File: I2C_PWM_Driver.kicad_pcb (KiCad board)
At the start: 2 copper layers, 89 x 42 mm, 97 parts, among them J1 Screw_Terminal_01x02, J2 Conn_01x02_Male, J3 Screw_Terminal_01x02, J4 Conn_02x08_Odd_Even, Q1 DMG2305UX, Q10 DMG2305UX, Q11 BC817, Q12 BC817, Q13 DMG2305UX, Q14 DMG2305UX, Q15 BC817, Q16 BC817, Q17 DMG2305UX, Q18 DMG2305UX, Q19 BC817, Q2 DMG2305UX, Q20 BC817, Q21 DMG2305UX, Q22 DMG2305UX, Q23 BC817, Q24 BC817, Q25 DMG2305UX, Q26 DMG2305UX, Q27 BC817, Q28 BC817, Q29 DMG2305UX, Q3 BC817, Q30 DMG2305UX, Q31 BC817, Q32 BC817, Q4 BC817, Q5 DMG2305UX, Q6 DMG2305UX, Q7 BC817, Q8 BC817, Q9 DMG2305UX, SW1 SW_Push, U1 PCA9685PW, U2 LM2931-5.0_SO8

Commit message: Silk updates
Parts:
- J3: footprint PWM_Conn:SCREW TERMINAL BLOCK 3.5MM 2POS -> Connector_PinHeader_2.54mm:PinHeader_1x02_P2.54mm_Vertical
- moved REF** 8.62 mm to (147.4, 87.4)
- moved J3 4.00 mm to (77.8, 80.3), turned to 0 degrees
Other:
- board text added: "+"
- board text added: "-"
- board text added: "0"
- board text added: "1"
- board text added: "10"
- board text added: "11"
- board text added: "12"
- board text added: "13"
- board text added: "14"
- board text added: "15"
- board text added: "2"
- board text added: "3"
- board text added: "4"
- board text added: "5"
- board text added: "6"
- board text added: "7"
- board text added: "8"
- board text added: "9"
- board text added: "PWM Out+"
- board text added: "SCL"
- board text added: "SDA"
- board text added: "Vin"

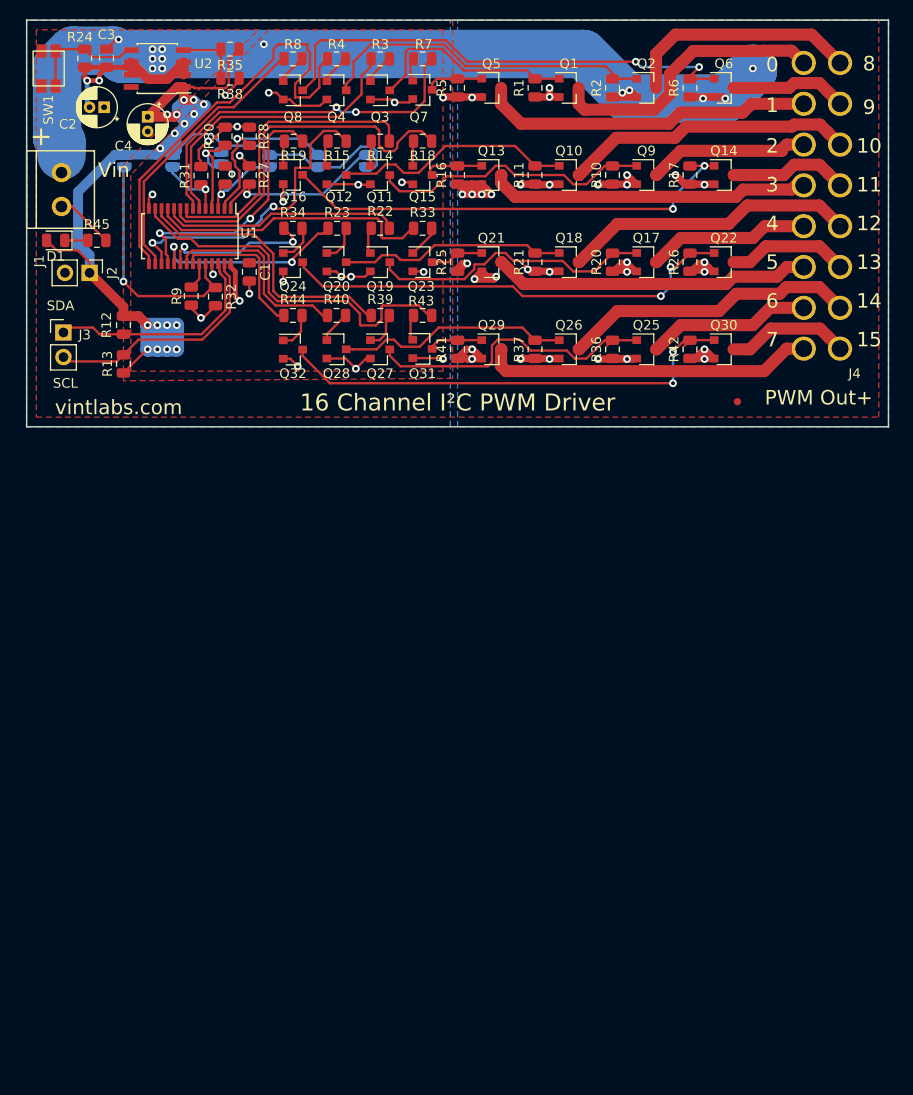
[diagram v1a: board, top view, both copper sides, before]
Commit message: Minmor silk updates
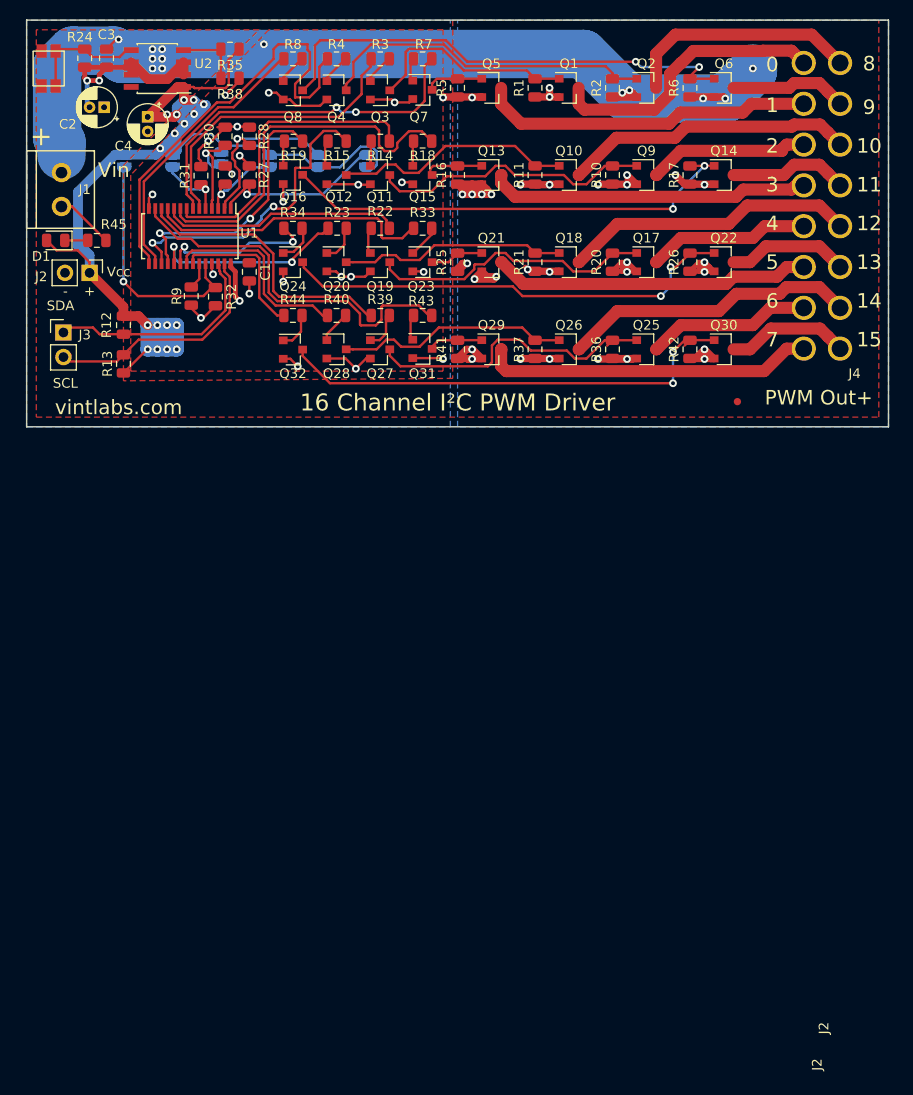
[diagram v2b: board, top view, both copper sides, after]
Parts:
- added ? (x2): , , F.Cu at (78.0, 76.0)
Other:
- board text added: "Vcc"
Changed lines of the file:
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@@
   (general
     (thickness 1.6)
-    (drawings 44)
+    (drawings 47)
     (tracks 1026)
     (zones 0)
-    (modules 97)
+    (modules 99)
     (nets 80)
   )
@@
     (add_net VCC)
   )
+  (module "" (layer F.Cu)
+    (at 78 76)
+    (fp_text reference "" (at 78 76) (layer F.SilkS)
+      (effects (font (size 1.27 1.27) (thickness 0.15)))
+    )
+    (fp_text value "" (at 78 76) (layer F.SilkS)
+      (effects (font (size 1.27 1.27) (thickness 0.15)))
+    )
+    (fp_text user J2 (at 78.33 76.1 90) (layer F.SilkS)
+      (effects (font (size 1 1) (thickness 0.15)))
+    )
+  )
+  (module "" (layer F.Cu)
+    (at 78 76)
+    (fp_text reference "" (at 77.8 80.26) (layer F.SilkS)
+      (effects (font (size 1.27 1.27) (thickness 0.15)))
+    )
+    (fp_text value "" (at 77.8 80.26) (layer F.SilkS)
+      (effects (font (size 1.27 1.27) (thickness 0.15)))
+    )
+    (fp_text user J2 (at 77.63 79.86 90) (layer F.SilkS)
+      (effects (font (size 1 1) (thickness 0.15)))
+    )
+  )
   (module Connector_PinHeader_2.54mm:PinHeader_1x02_P2.54mm_Vertical (layer F.Cu)
     (at 77.8 80.26)
@@
     (tags diode)
     (attr smd)
-    (fp_text reference D1 (at 0 -1.65 180) (layer F.SilkS)
+    (fp_text reference D1 (at 1.5 -1.65 180) (layer F.SilkS)
       (effects (font (size 1 1) (thickness 0.15)))
     )
@@
     (tags resistor)
     (attr smd)
-    (fp_text reference R45 (at 0 -1.65) (layer F.SilkS)
+    (fp_text reference R45 (at 1.75 -1.65) (layer F.SilkS)
       (effects (font (size 1 1) (thickness 0.15)))
     )
@@
   (module "PWM_Conn:SCREW TERMINAL BLOCK 3.5MM 2POS" (layer F.Cu)
     (at 74 65.5 270)
-    (fp_text reference J1 (at 7.4 -1.3 270) (layer F.SilkS)
+    (fp_text reference J1 (at 0 -6) (layer F.SilkS)
       (effects (font (size 1 1) (thickness 0.15)))
     )
@@
   (module "reset:EVQ Tactile Switch" (layer F.Cu)
     (at 76.275 53 270)
-    (fp_text reference SW1 (at 4.25 0.025 270) (layer F.SilkS)
+    (fp_text reference SW1 (at 4.25 0.025 270) (layer F.SilkS) hide
       (effects (font (size 1 1) (thickness 0.15)))
     )
@@
     (descr "Through hole straight pin header, 1x02, 2.54mm pitch, single row")
     (tags "Through hole pin header THT 1x02 2.54mm single row")
-    (fp_text reference J2 (at 0 -2.33 270) (layer F.SilkS)
+    (fp_text reference J2 (at 0.4 5) (layer F.SilkS)
       (effects (font (size 1 1) (thickness 0.15)))
     )
@@
       (solder_mask_margin 0.375) (clearance 0.375))
   )
+  (gr_text Vcc (at 83.5 74) (layer F.SilkS)
+    (effects (font (size 1 1) (thickness 0.15)))
+  )
+  (gr_text + (at 80.5 76) (layer F.SilkS)
+    (effects (font (size 1 1) (thickness 0.15)))
+  )
+  (gr_text - (at 78 76) (layer F.SilkS)
+    (effects (font (size 1 1) (thickness 0.15)))
+  )
   (gr_text SCL (at 78 85.5) (layer F.SilkS)

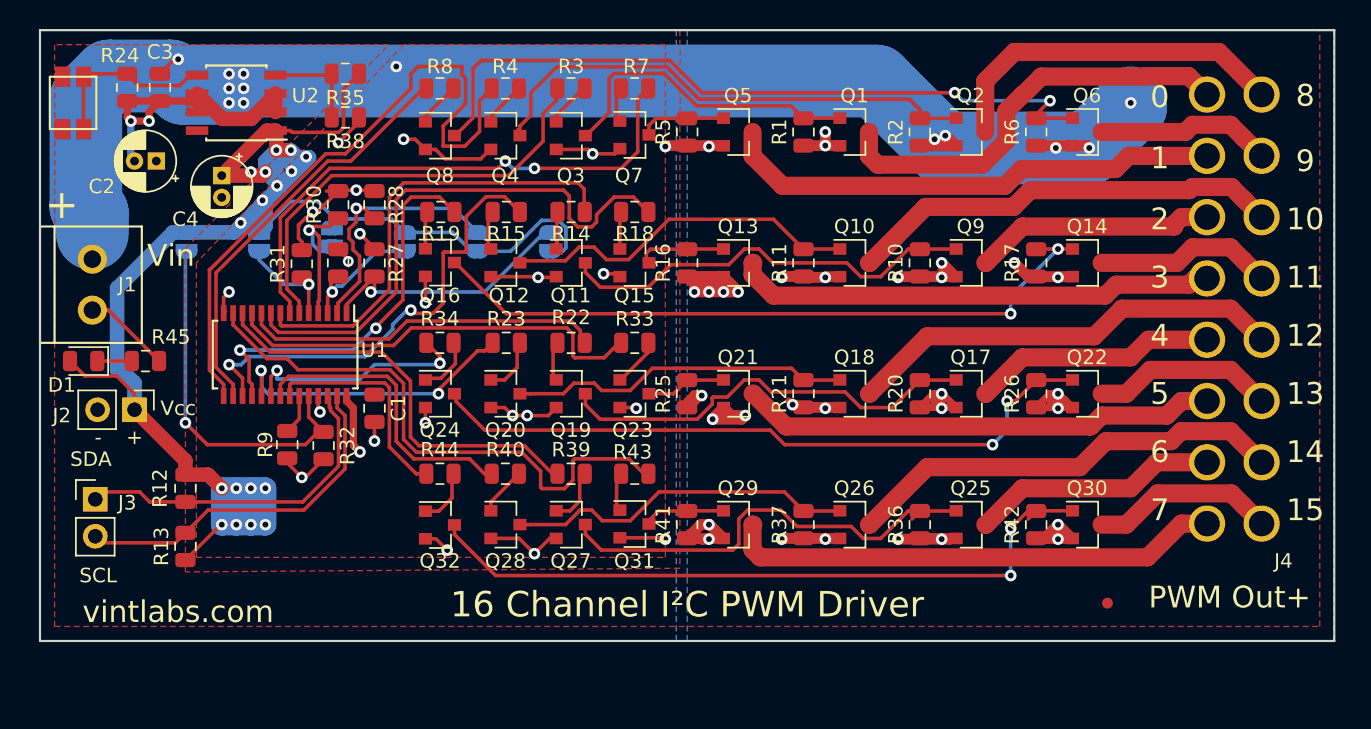
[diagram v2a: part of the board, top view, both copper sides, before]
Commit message: Fixed reversed SDA/SCL
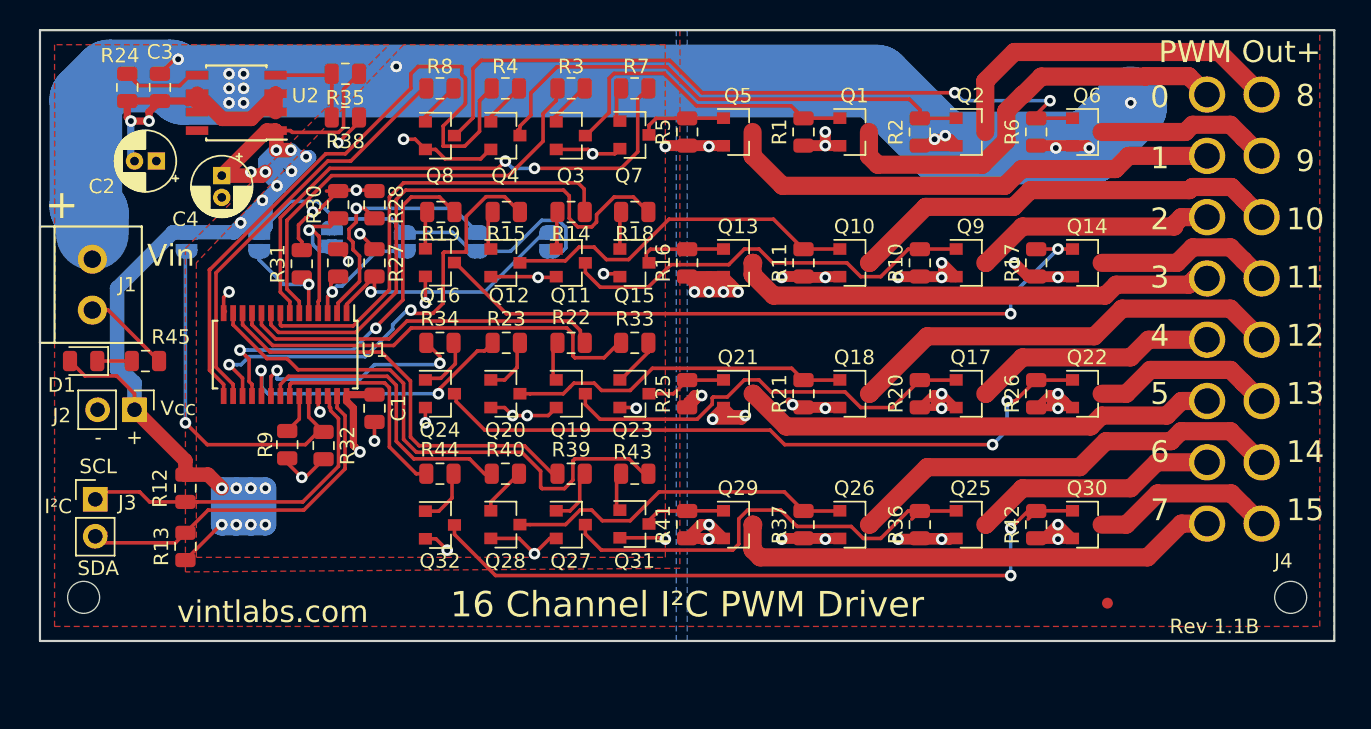
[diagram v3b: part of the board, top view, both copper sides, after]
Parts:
- removed the ? at (78.0, 76.0) (x2)
- removed SW1: SW_Push, reset:EVQ Tactile Switch
- added ? (x2): , , F.Cu at (78.0, 76.0)
- added REF**: MountingHole_2.2mm_M2_DIN965, MountingHole:MountingHole_2.2mm_M2_DIN965, F.Cu at (160.0, 87.0)
- added REF**: MountingHole_2.2mm_M2_DIN965, MountingHole:MountingHole_2.2mm_M2_DIN965, F.Cu at (77.0, 87.0)
- R1, R10, R11, R16, R17, R2, R20, R21, R25, R26, R36, R37, R41, R42, R5, R6: value R -> 1k
- R14, R15, R18, R19, R22, R23, R3, R33, R34, R39, R4, R40, R43, R44, R7, R8: value R -> 10k
- R38: value 68k -> 39k
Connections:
- J3 pad 1: SDA -> SCL
- J3 pad 2: SCL -> SDA
- R12 pad 2: SDA -> SCL
- R13 pad 2: SCL -> SDA
- U1 pad 26: SDA -> SCL
- U1 pad 27: SCL -> SDA
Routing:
- net Net-(R24-Pad1): track 12.1 -> 5.43 mm
- net SDA: track 23.4 -> 26.0 mm
- net SCL: track 26.0 -> 23.4 mm
- net VCC: track 133.2 -> 135.1 mm
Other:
- board text added: "I²C"
- board text added: "Rev 1.1B"
